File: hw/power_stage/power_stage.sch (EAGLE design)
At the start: 54 parts, among them IC1H MIC4420M, IC1L MIC4429M, IC2H MIC4420M, IC2L MIC4429M

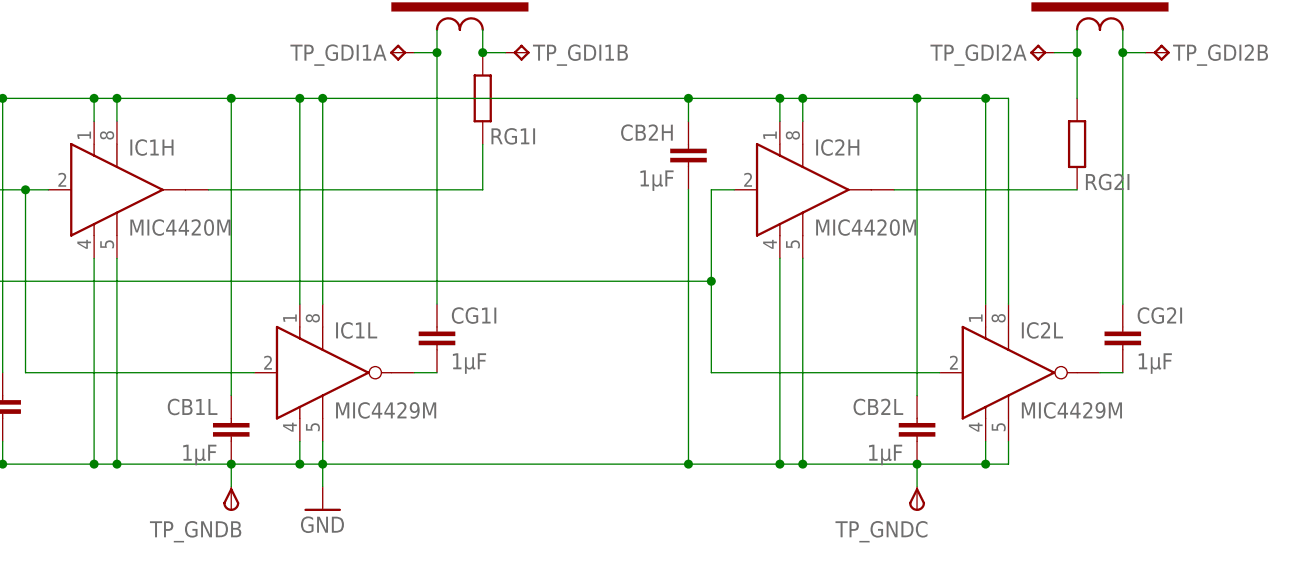
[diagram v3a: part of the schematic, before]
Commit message: Fix unconnected output pin on gate driver ICs
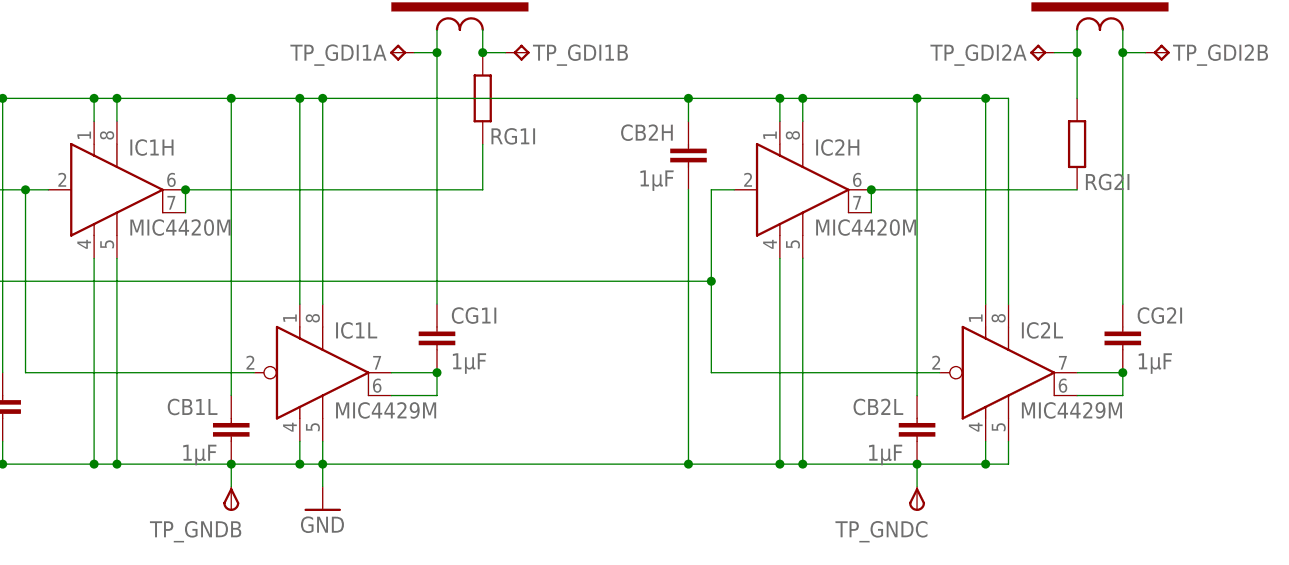
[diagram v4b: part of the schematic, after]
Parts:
- IC1H, IC2H: device transistor-power:MIC4420M -> induction-heater:MIC4420M
- IC1L, IC2L: device transistor-power:MIC4429M -> induction-heater:MIC4429M
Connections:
- net N$2: now also IC1H.OUT@2
- net N$22: now also IC1L.OUT@2
- net N$25: now also IC2L.OUT@2
- net N$4: now also IC2H.OUT@2
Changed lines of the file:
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@@
 <layer number="54" name="bGND_GNDA" color="1" fill="9" visible="no" active="no"/>
 <layer number="56" name="wert" color="7" fill="1" visible="no" active="no"/>
+<layer number="57" name="tCAD" color="7" fill="1" visible="no" active="no"/>
 <layer number="90" name="Modules" color="5" fill="1" visible="yes" active="yes"/>
 <layer number="91" name="Nets" color="2" fill="1" visible="yes" active="yes"/>
@@
 <layer number="108" name="tplace-old" color="10" fill="1" visible="yes" active="yes"/>
 <layer number="109" name="ref-old" color="11" fill="1" visible="yes" active="yes"/>
+<layer number="110" name="fp0" color="7" fill="1" visible="yes" active="yes"/>
+<layer number="111" name="LPC17xx" color="7" fill="1" visible="yes" active="yes"/>
+<layer number="112" name="tSilk" color="7" fill="1" visible="yes" active="yes"/>
+<layer number="113" name="IDFDebug" color="7" fill="1" visible="yes" active="yes"/>
 <layer number="116" name="Patch_BOT" color="9" fill="4" visible="yes" active="yes"/>
 <layer number="121" name="_tsilk" color="7" fill="1" visible="yes" active="yes"/>
 <layer number="122" name="_bsilk" color="7" fill="1" visible="yes" active="yes"/>
+<layer number="123" name="tTestmark" color="7" fill="1" visible="yes" active="yes"/>
+<layer number="124" name="bTestmark" color="7" fill="1" visible="yes" active="yes"/>
 <layer number="125" name="_tNames" color="7" fill="1" visible="yes" active="yes"/>
+<layer number="126" name="_bNames" color="7" fill="1" visible="yes" active="yes"/>
+<layer number="127" name="_tValues" color="7" fill="1" visible="yes" active="yes"/>
+<layer number="128" name="_bValues" color="7" fill="1" visible="yes" active="yes"/>
+<layer number="131" name="tAdjust" color="7" fill="1" visible="yes" active="yes"/>
+<layer number="132" name="bAdjust" color="7" fill="1" visible="yes" active="yes"/>
 <layer number="144" name="Drill_legend" color="7" fill="1" visible="yes" active="yes"/>
+<layer number="150" name="Notes" color="7" fill="1" visible="yes" active="yes"/>
 <layer number="151" name="HeatSink" color="7" fill="1" visible="yes" active="yes"/>
+<layer number="152" name="_bDocu" color="7" fill="1" visible="yes" active="yes"/>
+<layer number="153" name="FabDoc1" color="7" fill="1" visible="yes" active="yes"/>
+<layer number="154" name="FabDoc2" color="7" fill="1" visible="yes" active="yes"/>
+<layer number="155" name="FabDoc3" color="7" fill="1" visible="yes" active="yes"/>
 <layer number="199" name="Contour" color="7" fill="1" visible="yes" active="yes"/>
 <layer number="200" name="200bmp" color="1" fill="10" visible="yes" active="yes"/>
@@
 <layer number="223" name="223bmp" color="24" fill="1" visible="no" active="no"/>
 <layer number="224" name="224bmp" color="25" fill="1" visible="no" active="no"/>
+<layer number="248" name="Housing" color="7" fill="1" visible="yes" active="yes"/>
+<layer number="249" name="Edge" color="7" fill="1" visible="yes" active="yes"/>
 <layer number="250" name="Descript" color="3" fill="1" visible="no" active="no"/>
 <layer number="251" name="SMDround" color="12" fill="11" visible="no" active="no"/>
@@
 <part name="RP2L" library="rcl" deviceset="R-EU_" device="R0805"/>
 <part name="RP2H" library="rcl" deviceset="R-EU_" device="R0805"/>
-<part name="IC1H" library="transistor-power" deviceset="MIC4420" device="M"/>
-<part name="IC1L" library="transistor-power" deviceset="MIC4429" device="M"/>
-<part name="IC2H" library="transistor-power" deviceset="MIC4420" device="M"/>
-<part name="IC2L" library="transistor-power" deviceset="MIC4429" device="M"/>
+<part name="IC1H" library="induction-heater" deviceset="MIC4420" device="M"/>
+<part name="IC1L" library="induction-heater" deviceset="MIC4429" device="M"/>
+<part name="IC2H" library="induction-heater" deviceset="MIC4420" device="M"/>
+<part name="IC2L" library="induction-heater" deviceset="MIC4429" device="M"/>
 <part name="GND1" library="supply1" deviceset="GND" device=""/>
 <part name="DP1HA" library="diode" deviceset="ZENER-DIODE" device="SOD80C"/>
@@
 <segment>
 <pinref part="IC1L" gate="G$1" pin="OUT@1"/>
-<wire x1="-22.86" y1="-22.86" x2="-20.32" y2="-22.86" width="0.1524" layer="91"/>
+<wire x1="-25.4" y1="-25.4" x2="-20.32" y2="-25.4" width="0.1524" layer="91"/>
+<wire x1="-20.32" y1="-25.4" x2="-20.32" y2="-22.86" width="0.1524" layer="91"/>
 <pinref part="CG1I" gate="G$1" pin="2"/>
+<pinref part="IC1L" gate="G$1" pin="OUT@2"/>
+<wire x1="-20.32" y1="-22.86" x2="-25.4" y2="-22.86" width="0.1524" layer="91"/>
+<junction x="-20.32" y="-22.86"/>
 </segment>
 </net>
@@
 <segment>
 <pinref part="IC2L" gate="G$1" pin="OUT@1"/>
-<wire x1="55.88" y1="-22.86" x2="53.34" y2="-22.86" width="0.1524" layer="91"/>
+<wire x1="55.88" y1="-22.86" x2="55.88" y2="-25.4" width="0.1524" layer="91"/>
+<wire x1="55.88" y1="-25.4" x2="50.8" y2="-25.4" width="0.1524" layer="91"/>
 <pinref part="CG2I" gate="G$1" pin="2"/>
+<pinref part="IC2L" gate="G$1" pin="OUT@2"/>
+<wire x1="50.8" y1="-22.86" x2="55.88" y2="-22.86" width="0.1524" layer="91"/>
+<junction x="55.88" y="-22.86"/>
 </segment>
 </net>
@@
 <wire x1="-15.24" y1="2.54" x2="-15.24" y2="-2.54" width="0.1524" layer="91"/>
 <pinref part="IC1H" gate="G$1" pin="OUT@1"/>
-<wire x1="-15.24" y1="-2.54" x2="-45.72" y2="-2.54" width="0.1524" layer="91"/>
+<wire x1="-15.24" y1="-2.54" x2="-48.26" y2="-2.54" width="0.1524" layer="91"/>
+<pinref part="IC1H" gate="G$1" pin="OUT@2"/>
+<wire x1="-48.26" y1="-5.08" x2="-48.26" y2="-2.54" width="0.1524" layer="91"/>
+<junction x="-48.26" y="-2.54"/>
 </segment>
 </net>
@@
 <pinref part="IC2H" gate="G$1" pin="OUT@1"/>
 <pinref part="RG2I" gate="G$1" pin="1"/>
-<wire x1="30.48" y1="-2.54" x2="50.8" y2="-2.54" width="0.1524" layer="91"/>
-</segment>
-</net>
+<wire x1="27.94" y1="-2.54" x2="50.8" y2="-2.54" width="0.1524" layer="91"/>
+<pinref part="IC2H" gate="G$1" pin="OUT@2"/>
+<wire x1="27.94" y1="-5.08" x2="27.94" y2="-2.54" width="0.1524" layer="91"/>
+<junction x="27.94" y="-2.54"/>
+</segment>
+</net>

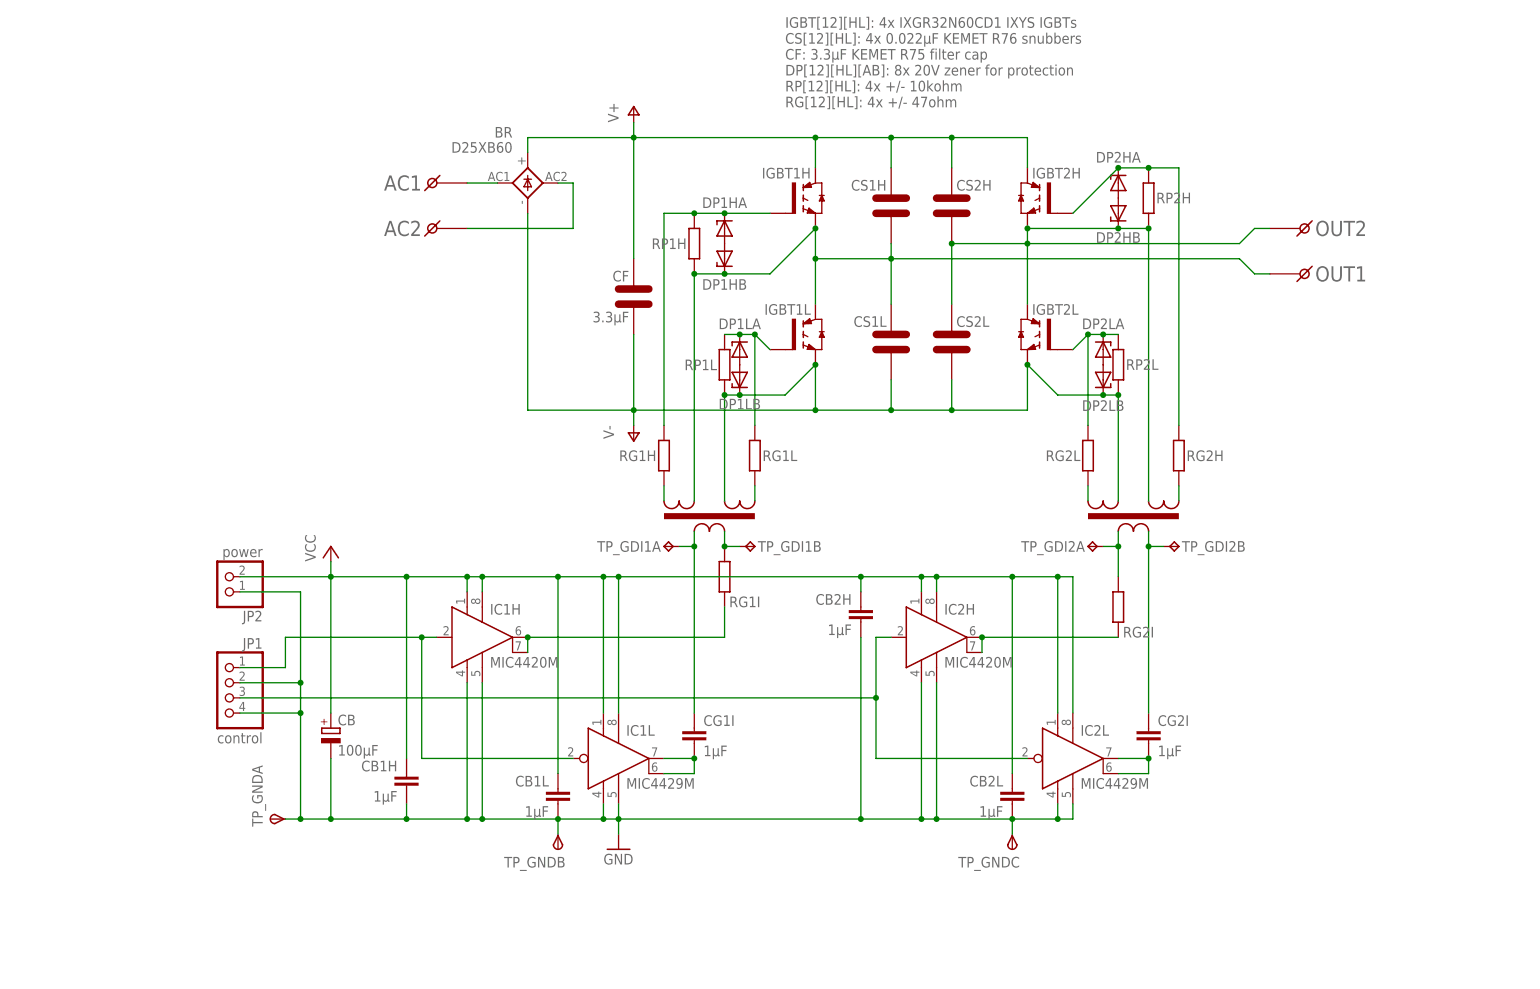
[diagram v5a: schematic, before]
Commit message: Clean up the power stage schematic
This means the board changed a bit too
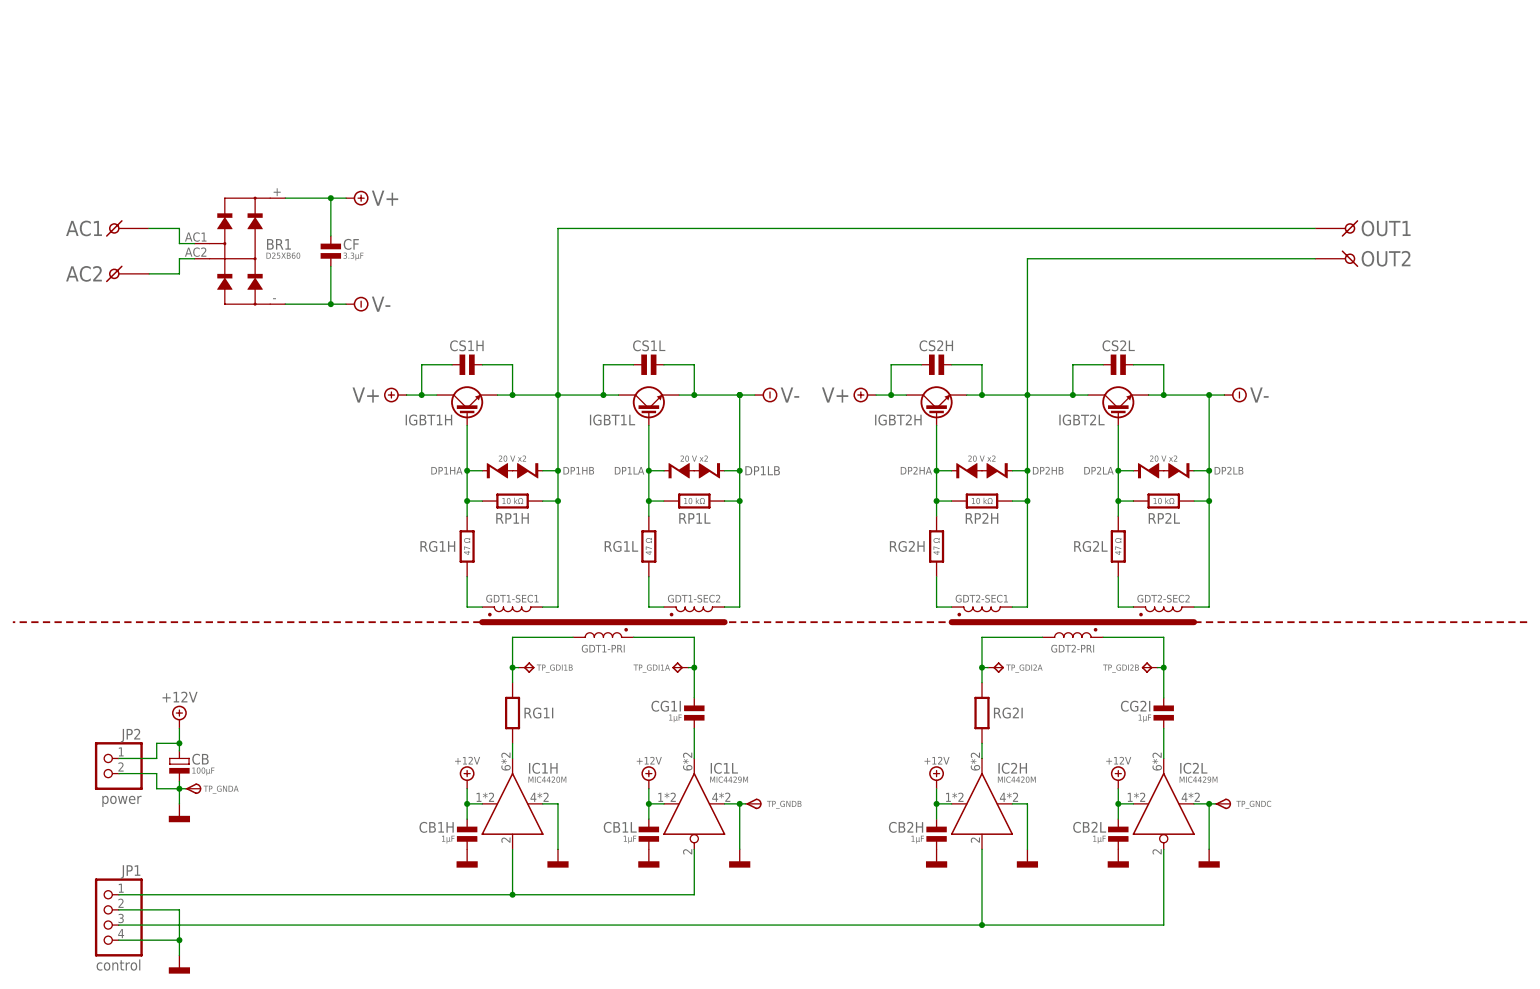
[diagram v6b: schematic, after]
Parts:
- removed BR: D25XB60, induction-heater:D25XB60
- added BR1: D25XB60, induction-heater:D25XB60
- CB: device rcl:CPOL-EUE2.5-7 -> passives:CPOL-PANASONIC-B
- CB1H, CB1L, CB2H, CB2L, CG1I, CG2I: device rcl:C-EUC0805 -> passives:C0805
- DP1HA, DP1HB, DP1LA, DP1LB, DP2HA, DP2HB, DP2LA, DP2LB: value (none) -> 20 V; device diode:ZENER-DIODESOD80C -> induction-heater:DIODE-ZENER-SOD80C
- RG1H, RG1L, RG2H, RG2L: value (none) -> 47 Ω; device rcl:R-EU_R0805 -> passives:R-0805
- RG1I, RG2I: device rcl:R-EU_R0805 -> passives:R-0805
- RP1H, RP1L, RP2H, RP2L: value (none) -> 10 kΩ; device rcl:R-EU_R0805 -> passives:R-0805
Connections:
- removed net VCC: CB.+, CB1H.1, CB1L.1, CB2H.1, CB2L.1, IC1H.VS, IC1H.VS1, IC1L.VS, IC1L.VS1, IC2H.VS, IC2H.VS1, IC2L.VS, IC2L.VS1, JP2.2
- new net +12V: CB.+, CB1H.1, CB1L.1, CB2H.1, CB2L.1, IC1H.VS, IC1L.VS, IC2H.VS, IC2L.VS, JP2.1
- net AC1: now also BR1.AC1; no longer BR.AC1
- net AC2: now also BR1.AC2; no longer BR.AC2
- net GND: now also JP2.2; no longer IC1H.GND1, IC1L.GND1, IC2H.GND1, IC2L.GND1, JP2.1
- net N$1: now also GDT1-PRI.2; no longer GDT1.PB
- net N$12: now also GDT2-SEC2.1; no longer GDT2.S2B
- net N$13: now also GDT2-SEC1.1; no longer GDT2.S1A
- net N$2: now also IC1H.OUT; no longer IC1H.OUT@1, IC1H.OUT@2
- net N$22: no longer IC1L.OUT@2
- net N$25: no longer IC2L.OUT@2
- net N$26: now also GDT1-PRI.1; no longer GDT1.PA
- net N$27: now also GDT2-PRI.1; no longer GDT2.PA
- net N$3: now also GDT1-SEC1.1; no longer GDT1.S1A
- net N$4: now also IC2H.OUT; no longer IC2H.OUT@1, IC2H.OUT@2
- net N$5: now also GDT2-PRI.2; no longer GDT2.PB
- net N$7: now also GDT1-SEC2.1; no longer GDT1.S2B
- net OUT1: now also CS1H.P$2, CS1L.P$1, GDT1-SEC1.2; no longer CS1H.P$1, CS1L.P$2, GDT1.S1B
- net OUT2: now also CS2H.P$2, CS2L.P$1, GDT2-SEC1.2; no longer CS2H.P$1, CS2L.P$2, GDT2.S1B
- net V+: now also BR1.+, CF.P$1, CS1H.P$1, CS2H.P$1; no longer BR.+, CF.P$2, CS1H.P$2, CS2H.P$2
- net V-: now also BR1.-, CF.P$2, CS1L.P$2, CS2L.P$2, GDT1-SEC2.2, GDT2-SEC2.2; no longer BR.-, CF.P$1, CS1L.P$1, CS2L.P$1, GDT1.S2A, GDT2.S2A
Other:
- note added: "20 V x2"
- note added: "IGBT[12][HL]: 4x IXGR32N60CD1 IXYS IGBTs CS[12][HL]: 4x 0.022µF KEMET R76 snubbers CF: 3.3µF KEMET R75 filter cap"
- note removed: "IGBT[12][HL]: 4x IXGR32N60CD1 IXYS IGBTs CS[12][HL]: 4x 0.022µF KEMET R76 snubbers CF: 3.3µF KEMET R75 filter cap DP[12][HL][AB]: 8x 20V zener for protection RP[12][HL]: 4x +/- 10kohm RG[12][HL]: 4x +/- 47ohm"
- moved on the sheet: CF, CS1H, CS1L, CS2H, CS2L, JP1, JP2, RG1H, RG1I, RG1L, RG2H, RG2I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

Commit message: Changed power stage PCB connectors
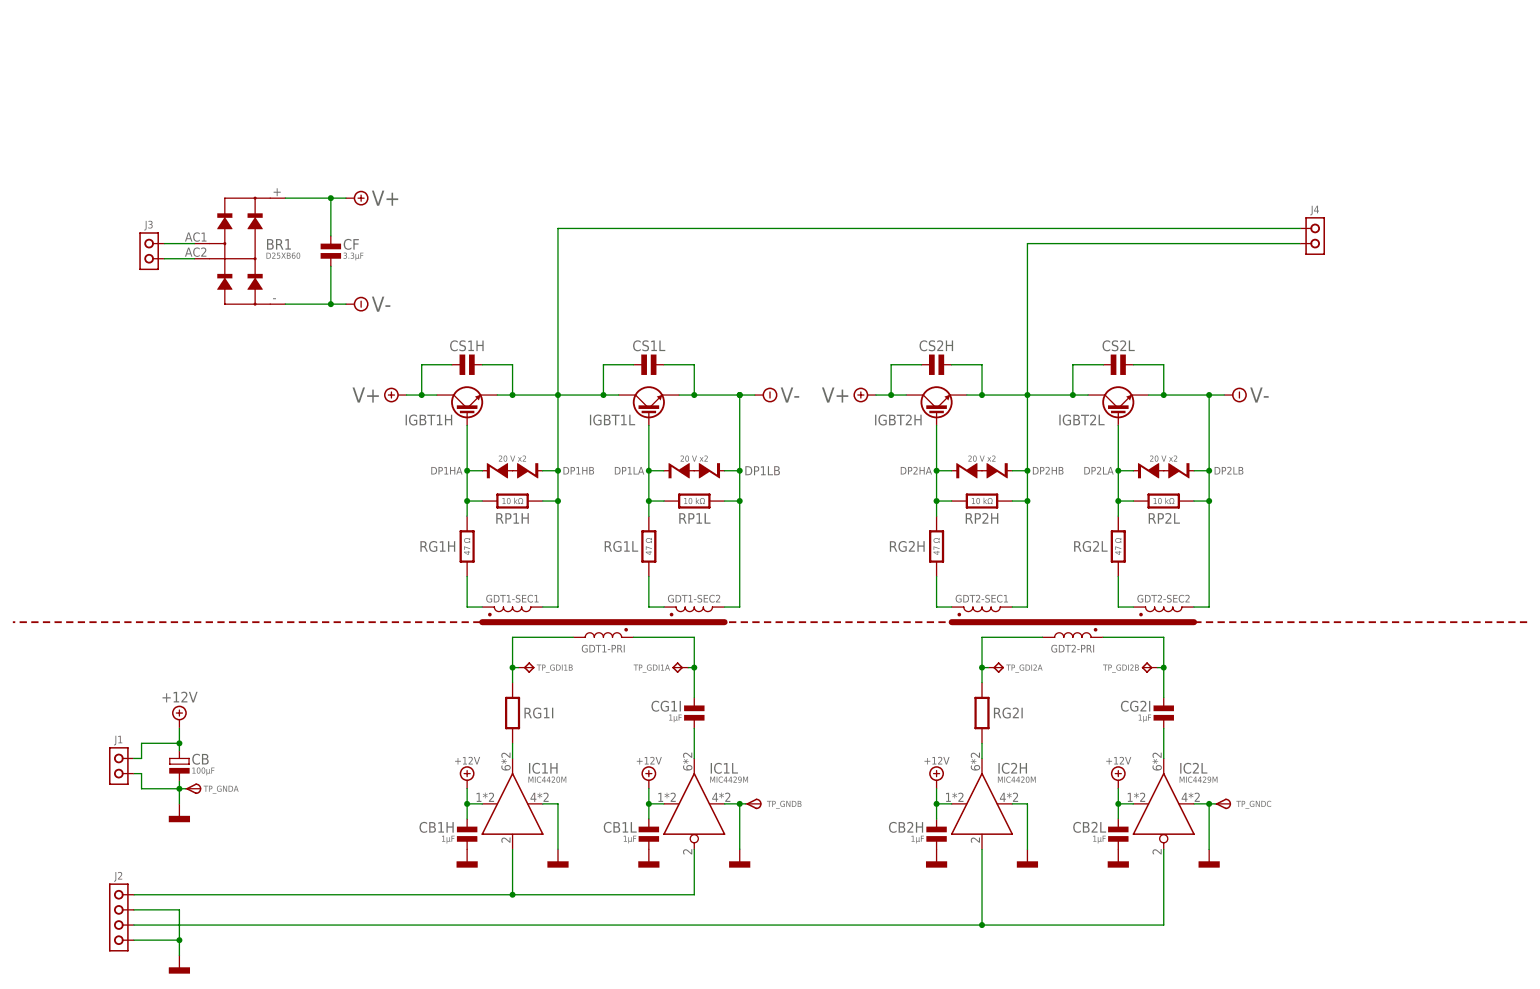
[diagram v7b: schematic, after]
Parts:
- removed AC1: AC1, induction-heater:SCREW
- removed AC2: AC2, induction-heater:SCREW
- removed JP1: control, pinhead:PINHD-1X4
- removed JP2: power, pinhead:PINHD-1X2
- removed OUT1: OUT1, induction-heater:SCREW
- removed OUT2: OUT2, induction-heater:SCREW
- added J1: CON-2POS-NS25, induction-heater:CON-2POS-NS25
- added J2: CON-4POS-NS25, induction-heater:CON-4POS-NS25
- added J3, J4: CON-2POS-MNL, induction-heater:CON-2POS-MNL
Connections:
- net +12V: now also J1.1; no longer JP2.1
- net AC1: now also J3.1; no longer AC1.1
- net AC2: now also J3.2; no longer AC2.1
- net GND: now also J1.2, J2.2, J2.4; no longer JP1.2, JP1.4, JP2.2
- net N$15: now also J2.1; no longer JP1.1
- net N$20: now also J2.3; no longer JP1.3
- net OUT1: now also J4.1; no longer OUT1.1
- net OUT2: now also J4.2; no longer OUT2.1
